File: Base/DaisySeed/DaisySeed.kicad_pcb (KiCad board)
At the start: 2 copper layers, 30 x 84 mm, 33 parts, among them J1 Barrel_Jack_Switch, J2 Conn_01x04_Pin, J3 Conn_01x04_Pin, J4 AudioJack2_Ground, J5 AudioJack2_Ground, J6 Conn_01x04_Pin, J7 Conn_01x04_Pin, Q1 BC846, Q2 LS844, Q3 PMV250, SW1 SW_SPDT, SW2 SW_Push

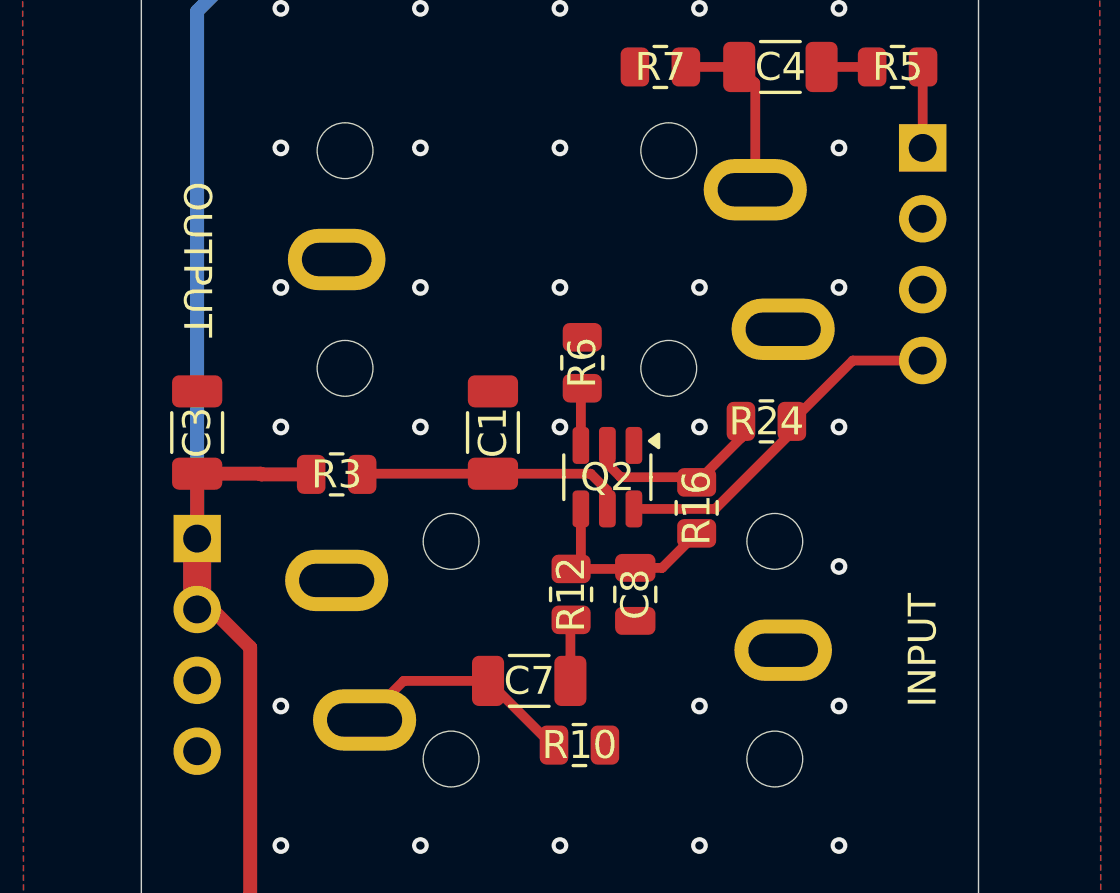
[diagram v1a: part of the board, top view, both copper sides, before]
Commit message: Add input signal re-biasing to the Daisy Seed after all
Yes, the Daisy Seed ends up AC-coupling the input, and will re-bias it
to the mid-point of the analog voltage range for the audio codec.

But thinking some more about it, I started worrying about the capacitor
used. In particular, it might very well be a low-voltage one, and the
dual JFET input will have a buffered output voltage in the 5V+ range.

Simulation puts the signal level centered at 7.4V, but who knows what an
actual LS844 will be.  For all I know the dual JFET thing really would
want more of a voltage range than a 9V positive supply and it will not
work very well in real life, but we'll see.

[ I can always go back to the single MMBF5103 as an input buffer, that
  worked fine and is more than sufficient for a guitar pedal -
  particularly one of my design.

  The whole "let's used two matched JFET's" is really me being rather
  silly, after having seen reports of it having particularly good THD by
  Rod Elliott (ESP) [1] and Erno Borbely [2].

  ESP uses the matched JFET as a current source, Erno Borbely as a
  current sink. Mostly it shouldn't make any difference, but I randomly
  did the current sink thing. And that does end up with the signal at a
  higher voltage ]

Regardless, it's entirely possible that the AC coupling on the Daisy
Seed uses a capacitor that is rated for something like 6.3V, which is
common for smaller SMT caps.  That would make sense, since the
assumption is an incoming signal around ground, with the center of the
analog voltage at 1.6V.

So my assumption that the AC coupling of the Daisy Seed would make it
unnecessary to do any AC coupling on the base board signal was clearly
horribly flawed.  Let's fix it.

I wonder what the next horribly flawed idea is?

Link: https://sound-au.com/articles/jfet-design.htm#s5 [1]
Link: https://pearl-hifi.com/06_Lit_Archive/14_Books_Tech_Papers/Borbely_Erno/JFETS_The_New_Frontier.pdf [2]
Signed-off-by: Linus Torvalds <torvalds@linux-foundatio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
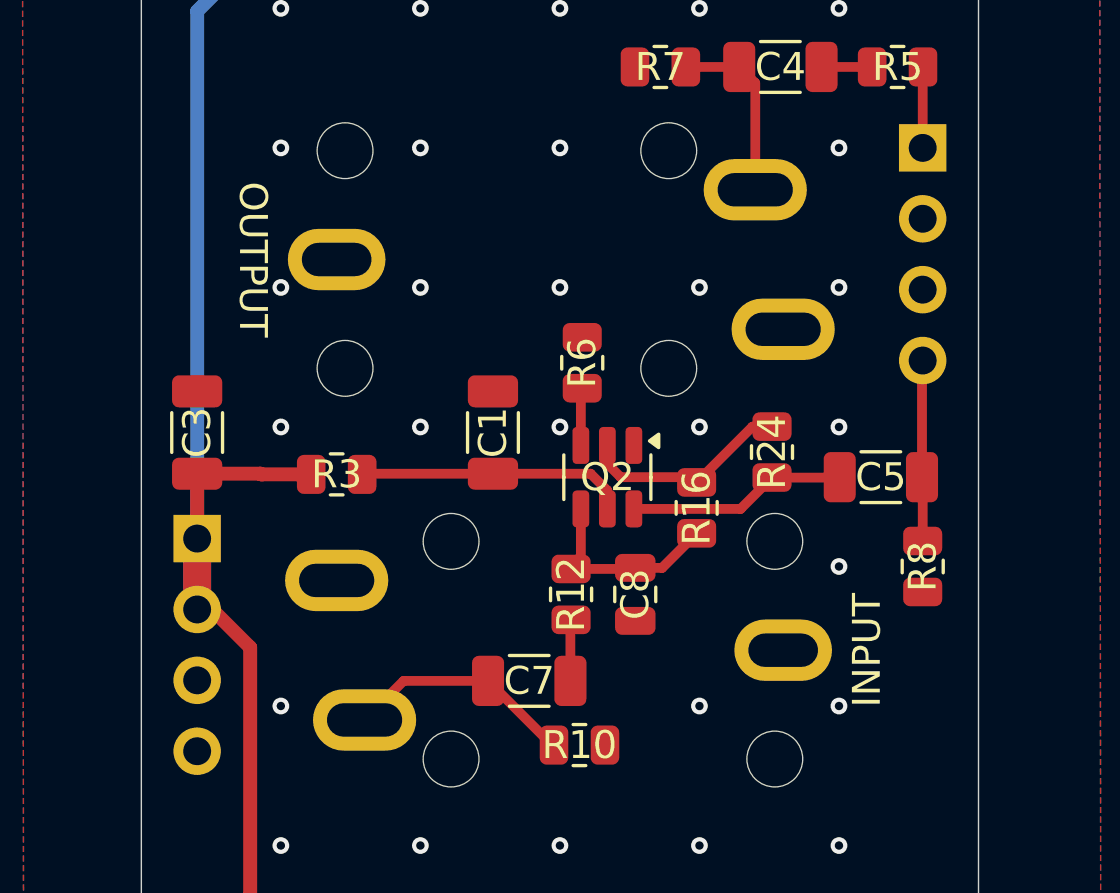
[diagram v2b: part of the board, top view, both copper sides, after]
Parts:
- added C5: 0.47uF, Capacitor_SMD:C_1206_3216Metric, F.Cu at (111.5, 111.8)
- added R8: 1MEG, Resistor_SMD:R_0805_2012Metric, F.Cu at (113.0, 115.0)
- moved R24 1.12 mm to (107.6, 110.9), turned to 90 degrees
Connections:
- Q2 pad 6: IN^{EFF} -> Net-(Q2B-S)
- R24 pad 1: IN^{EFF} -> Net-(Q2B-S)
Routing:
- net Net-(Q2B-S): track 0.00 -> 7.85 mm
- net IN^{EFF}: track 12.8 -> 6.49 mm
- net Net-(Q2A-D): track 6.29 -> 6.98 mm

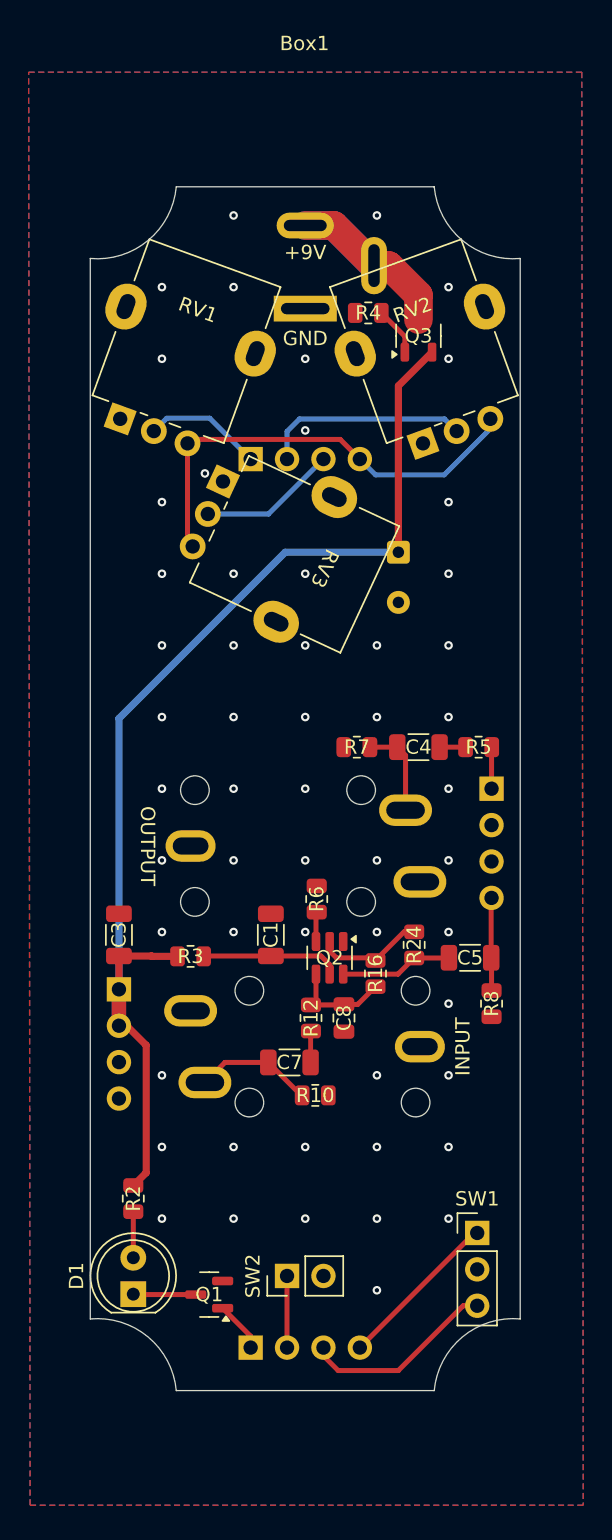
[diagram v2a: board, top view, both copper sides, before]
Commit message: Try attaching the Daisy Seed directly on the base board
Ok, so to fit this thing, I needed to play some games, and also get rid
of the third potentiometer.

So now it only has two pots, and the Daisy Seed needs to be the
unsoldered kind, where you solder low-profile pin headers to the "wrong"
side of the board.

IOW, the Daisy Seed gets mounted upside down on the top of the base
board, and then it kind of fits.

I say "kind of", because this is all without a stomp switch.  I haven't
decided on what I want to do about that.  The switch connector is just
holes for a pin header - or more likely, two wires.

I do think I should just give up on the 1950A form factor, which would
make all these games a complete non-issue.  But it's not like the whole
thing makes any sense to begin with, so why start being sensible now?

Signed-off-by: Linus Torvalds <torvalds@linux-foundation.org>
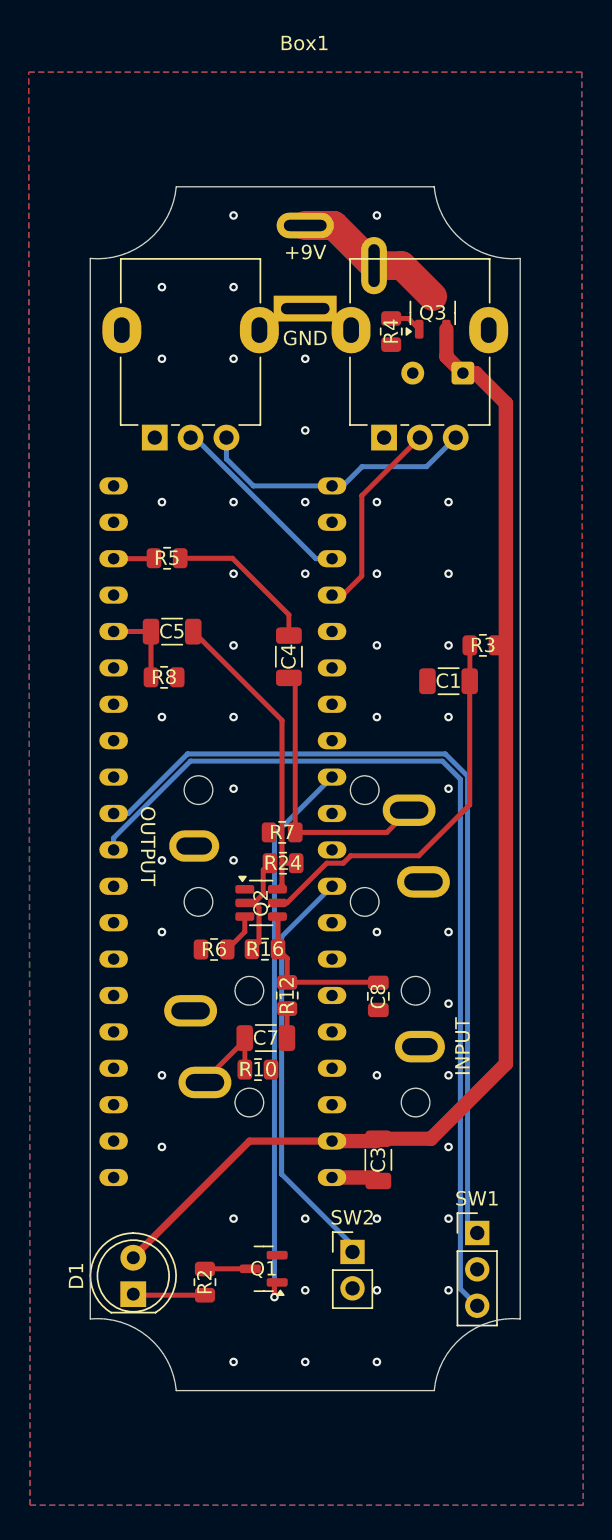
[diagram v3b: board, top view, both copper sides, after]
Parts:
- removed J2, J3, J6, J7: Conn_01x04_Pin, Connector_PinHeader_2.54mm:PinHeader_1x04_P2.54mm_Vertical
- removed RV3: 10k, Mylib:Potentiometer_9mm_MP
- added U201: Daisy Seed, Mylib:DaisySeed, B.Cu at (94.2, 103.0)
- moved R8 32.3 mm to (90.2, 92.2), turned to 0 degrees
- moved C5 30.8 mm to (90.7, 89.0), turned to 180 degrees
- moved R3 29.8 mm to (112.4, 90.0), turned to 180 degrees
- moved R5 25.4 mm to (90.4, 83.9), turned to 0 degrees
- moved C3 24.0 mm to (105.1, 125.9), turned to -90 degrees
- moved C1 21.6 mm to (110.0, 92.5), turned to 180 degrees
- moved C2 13.3 mm to (111.0, 71.0), turned to 180 degrees
- moved C4 11.0 mm to (98.9, 90.8), turned to -90 degrees
- moved R24 10.8 mm to (98.5, 105.2), turned to 180 degrees
- moved R6 7.98 mm to (93.6, 111.2), turned to 180 degrees
- moved R7 7.91 mm to (98.4, 103.0)
- moved R16 7.90 mm to (97.2, 111.2), turned to 180 degrees
- moved R2 7.68 mm to (93.0, 134.4), turned to 90 degrees
- moved Q2 6.13 mm to (96.9, 108.0), turned to 0 degrees
- moved SW2 4.87 mm to (103.3, 132.3), turned to 0 degrees
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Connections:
- net +V renamed +VA
- net Net-(J2-Pin_4) renamed +3.3VA
- D1 pad 2: Net-(D1-A) -> VIN
- Q1 pad 3: Net-(D1-K) -> Net-(Q1-C)
- R2 pad 1: VIN -> Net-(D1-K)
- R2 pad 2: Net-(D1-A) -> Net-(Q1-C)
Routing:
- net SW_UP: track 13.6 -> 65.0 mm
- net SW_DOWN: track 11.5 -> 59.2 mm
- net LED: track 3.56 -> 39.1 mm, vias 0 -> 1
- net FOOTSWITCH: track 5.00 -> 29.0 mm
- net +3.3VA: track 39.0 -> 19.7 mm
- net +VA: track 9.71 -> 27.4 mm
- net Net-(Q2B-S): track 7.85 -> 21.7 mm
- net OUT^{CONN}: track 6.55 -> 19.6 mm
- net POT3: track 9.65 -> 0.00 mm
- net Net-(C4-Pad1): track 1.81 -> 10.7 mm
- net POT1: track 8.31 -> 14.1 mm
- net Net-(Q2B-G): track 7.32 -> 11.3 mm
- net GND: track 0.00 -> 3.33 mm, vias 55 -> 47
- net Net-(D1-A): track 3.22 -> 0.00 mm
- net Net-(Q1-C): track 0.00 -> 3.17 mm
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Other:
- board text added: "Daisy Seed upside down other side!"
